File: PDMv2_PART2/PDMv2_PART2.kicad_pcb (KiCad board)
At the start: 4 copper layers, 60 x 40 mm, 4 parts

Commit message: Layout done
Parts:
- removed the REF** at (171.0, 81.0)
- removed the REF** at (121.0, 111.0)
- removed the REF** at (121.0, 81.0)
- added J1: TVP00WCI17-02P, Connector:tvp00wci17-02p, F.Cu at (81.6, 91.0)
- added J2: UMPS-08-X-X-V-S-W, UMPS-08-05.5-G-V-S-W-TR:SAMTEC_UMPS-08-X-X-V-S-W, F.Cu at (61.5, 72.3)
- added J3: UMPS-08-X-X-V-S-W, UMPS-08-05.5-G-V-S-W-TR:SAMTEC_UMPS-08-X-X-V-S-W, F.Cu at (61.5, 109.5)
- added REF**: MountingHole_3mm_Pad_Via, MountingHole:MountingHole_3mm_Pad_Via, F.Cu at (97.8, 63.7)
- added REF**: MountingHole_3mm_Pad_Via, MountingHole:MountingHole_3mm_Pad_Via, F.Cu at (98.0, 118.5)
- moved REF** 111.1 mm to (61.8, 91.0)
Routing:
- net /TSAL/HV: vias 0 -> 29
- net /SDC/ASMS: vias 0 -> 12
- net /REARBOX/DIAGPORT/BRAKE_L: vias 0 -> 26
- net /PUMP2: vias 0 -> 26
- net /PUMP1: vias 0 -> 23
- net /PC4: vias 0 -> 14
- net /PC3: vias 0 -> 13
- net /PC2: vias 0 -> 13
- net /PC1: vias 0 -> 12
- net /INVERTER 2: vias 0 -> 18
- net /INVERTER 1: vias 0 -> 21
- net /FBOX: vias 0 -> 15
- net /FAN2: vias 0 -> 34
- net /FAN1: vias 0 -> 17
- net /DASH: vias 0 -> 13
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- added copper zone on B.Cu, net /BRAKE/IR/AIR
- added copper zone on F.Cu, net /BRAKE/IR/AIR
- added copper zone on In1.Cu, net /BRAKE/IR/AIR
- added copper zone on In2.Cu, net /BRAKE/IR/AIR
- added copper zone on B.Cu, net /DASH
- added copper zone on F.Cu, net /DASH
- added copper zone on In1.Cu, net /DASH
- added copper zone on In2.Cu, net /DASH
- added copper zone on B.Cu, net /FAN1
- added copper zone on F.Cu, net /FAN1
- added copper zone on In1.Cu, net /FAN1
- added copper zone on In2.Cu, net /FAN1
- added copper zone on B.Cu, net /FAN2
- added copper zone on F.Cu, net /FAN2
- added copper zone on In1.Cu, net /FAN2
- added copper zone on In2.Cu, net /FAN2
- added copper zone on B.Cu, net /FBOX
- added copper zone on F.Cu, net /FBOX
- added copper zone on In1.Cu, net /FBOX
- added copper zone on In2.Cu, net /FBOX
- added copper zone on B.Cu, net /INVERTER 1
- added copper zone on F.Cu, net /INVERTER 1
- added copper zone on In1.Cu, net /INVERTER 1
- added copper zone on In2.Cu, net /INVERTER 1
- added copper zone on B.Cu, net /INVERTER 2
- added copper zone on F.Cu, net /INVERTER 2
- added copper zone on In1.Cu, net /INVERTER 2
- added copper zone on In2.Cu, net /INVERTER 2
- added copper zone on B.Cu, net /PC1
- added copper zone on F.Cu, net /PC1
- added copper zone on In1.Cu, net /PC1
- added copper zone on In2.Cu, net /PC1
- added copper zone on B.Cu, net /PC2
- added copper zone on F.Cu, net /PC2
- added copper zone on In1.Cu, net /PC2
- added copper zone on In2.Cu, net /PC2
- added copper zone on B.Cu, net /PC3
- added copper zone on F.Cu, net /PC3
- added copper zone on In1.Cu, net /PC3
- added copper zone on In2.Cu, net /PC3
- added copper zone on B.Cu, net /PC4
- added copper zone on F.Cu, net /PC4
- added copper zone on In1.Cu, net /PC4
- added copper zone on In2.Cu, net /PC4
- added copper zone on B.Cu, net /PUMP1
- added copper zone on F.Cu, net /PUMP1
- added copper zone on In1.Cu, net /PUMP1
- added copper zone on In2.Cu, net /PUMP1
- added copper zone on B.Cu, net /PUMP2
- added copper zone on F.Cu, net /PUMP2
- added copper zone on In1.Cu, net /PUMP2
- added copper zone on In2.Cu, net /PUMP2
- added copper zone on B.Cu, net /REARBOX/DIAGPORT/BRAKE_L
- added copper zone on F.Cu, net /REARBOX/DIAGPORT/BRAKE_L
- added copper zone on In1.Cu, net /REARBOX/DIAGPORT/BRAKE_L
- added copper zone on In2.Cu, net /REARBOX/DIAGPORT/BRAKE_L
- added copper zone on B.Cu, net /SDC/ASMS
- added copper zone on F.Cu, net /SDC/ASMS
- added copper zone on In1.Cu, net /SDC/ASMS
- added copper zone on In2.Cu, net /SDC/ASMS
- added copper zone on B.Cu, net /TSAL/HV
- added copper zone on F.Cu, net /TSAL/HV
- added copper zone on In1.Cu, net /TSAL/HV
- added copper zone on In2.Cu, net /TSAL/HV
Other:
- board size 60 x 40 mm -> 43.5 x 62 mm
- board text removed: "Template"
- board text removed: "v${REVISION}"

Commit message: Fixes
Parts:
- moved J2 0.10 mm to (61.5, 72.5)
- moved J3 0.10 mm to (61.5, 109.4)
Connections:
- J1 pad 9: /DASH -> /SDC/ASMS

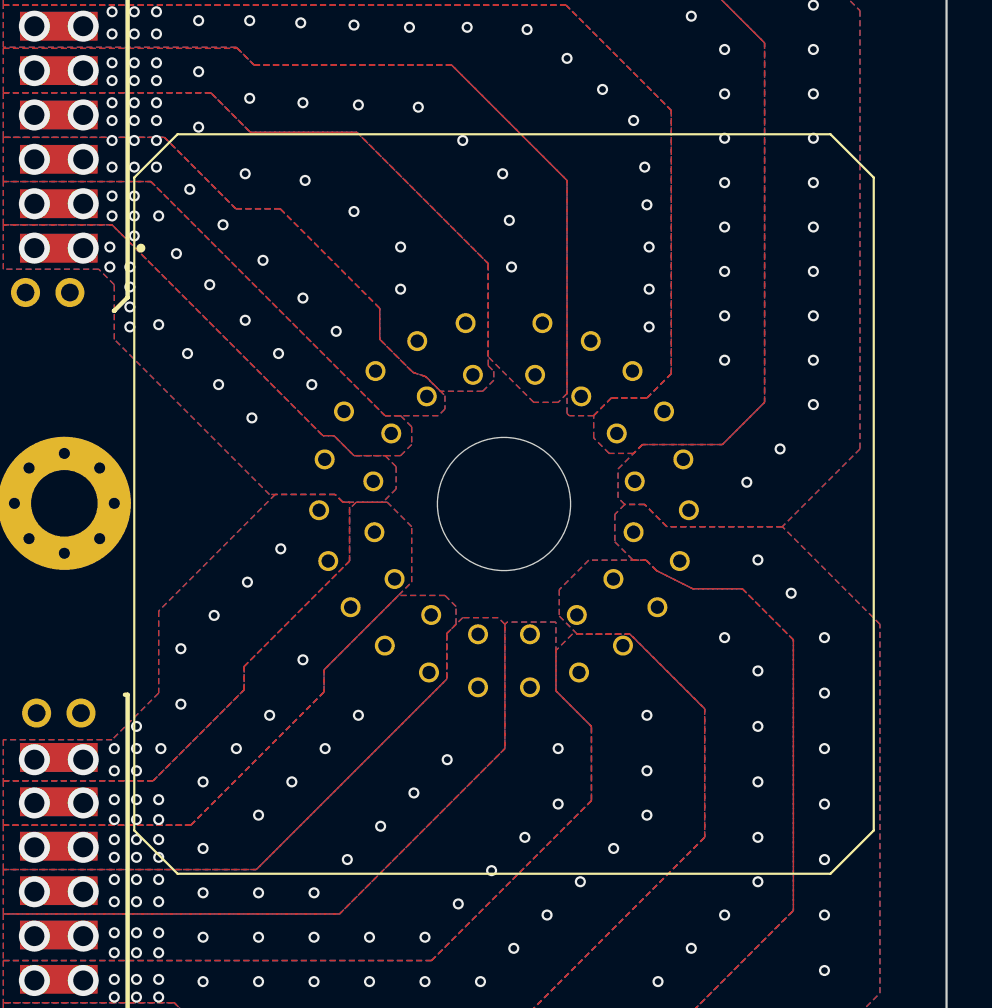
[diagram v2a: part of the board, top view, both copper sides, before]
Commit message: Fixes
Rotated connector footprint
Changed labels
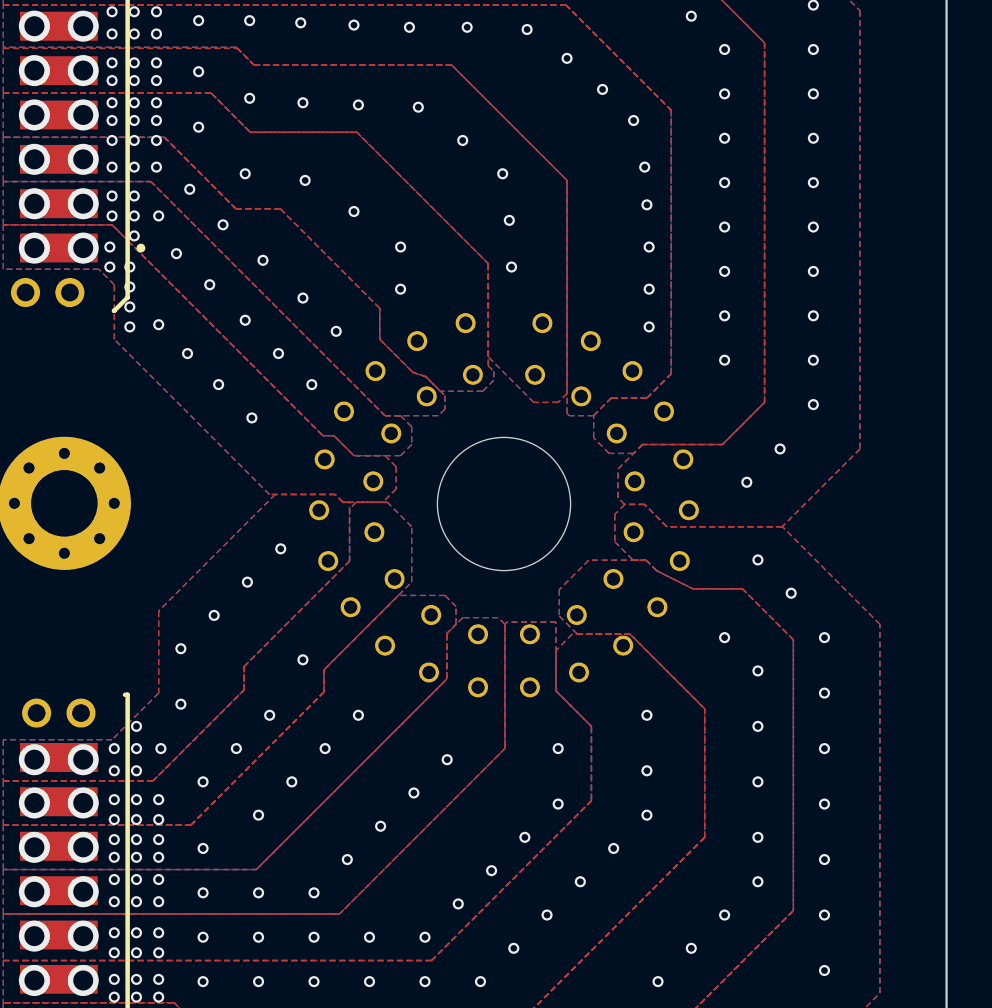
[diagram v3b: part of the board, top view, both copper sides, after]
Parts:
- J1: moved to B.Cu
- turned J1 to 180 degrees
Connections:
- J1 pad 10: /DASH -> /TSAL/HV
- J1 pad 11: /DASH -> /FAN2
- J1 pad 12: /PC1 -> /FAN2
- J1 pad 13: /PC1 -> /FAN2
- J1 pad 14: /PC2 -> /PUMP2
- J1 pad 15: /PC2 -> /PUMP2
- J1 pad 16: /PC3 -> /PUMP1
- J1 pad 17: /PC3 -> /PUMP1
- J1 pad 18: /PC4 -> /PUMP1
- J1 pad 19: /PC4 -> /FAN1
- J1 pad 2: /FBOX -> /INVERTER 2
- J1 pad 20: /PC4 -> /FAN1
- J1 pad 21: /FAN1 -> /PC4
- J1 pad 22: /FAN1 -> /PC4
- J1 pad 23: /PUMP1 -> /PC4
- J1 pad 24: /PUMP1 -> /PC3
- J1 pad 25: /PUMP1 -> /PC3
- J1 pad 26: /PUMP2 -> /PC2
- J1 pad 27: /PUMP2 -> /PC2
- J1 pad 28: /FAN2 -> /PC1
- J1 pad 29: /FAN2 -> /PC1
- J1 pad 3: /FBOX -> /INVERTER 2
- J1 pad 30: /FAN2 -> /DASH
- J1 pad 31: /TSAL/HV -> /SDC/ASMS
- J1 pad 32: /TSAL/HV -> /DASH
- J1 pad 33: /REARBOX/DIAGPORT/BRAKE_L -> /SDC/ASMS
- J1 pad 34: /REARBOX/DIAGPORT/BRAKE_L -> /SDC/ASMS
- J1 pad 35: /REARBOX/DIAGPORT/BRAKE_L -> /BRAKE/IR/AIR
- J1 pad 36: /INVERTER 1 -> /BRAKE/IR/AIR
- J1 pad 37: /INVERTER 2 -> /FBOX
- J1 pad 38: /INVERTER 1 -> /BRAKE/IR/AIR
- J1 pad 39: /INVERTER 2 -> /FBOX
- J1 pad 4: /BRAKE/IR/AIR -> /INVERTER 1
- J1 pad 5: /BRAKE/IR/AIR -> /REARBOX/DIAGPORT/BRAKE_L
- J1 pad 6: /BRAKE/IR/AIR -> /INVERTER 1
- J1 pad 7: /SDC/ASMS -> /REARBOX/DIAGPORT/BRAKE_L
- J1 pad 8: /SDC/ASMS -> /REARBOX/DIAGPORT/BRAKE_L
- J1 pad 9: /SDC/ASMS -> /TSAL/HV

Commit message: Production
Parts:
- added G***: LOGO, logos:PUTM_LOGO_15mm, F.Cu at (97.8, 92.5)
- added G***: LOGO, Logos:SignatureBox25mm, F.Cu at (79.4, 116.3)
- moved REF** 1.60 mm to (96.4, 118.3)
- moved REF** 1.34 mm to (96.4, 63.7)
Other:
- board size 43.5 x 62 mm -> 42.5 x 62 mm
- board text added: "Kacper Biadała"
- board text added: "PDM"
- board text added: "v2.0"

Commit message: Connector pads renumbered
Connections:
- J1 pad 10: /TSAL/HV -> /BRAKE/IR/AIR
- J1 pad 11: /FAN2 -> /FBOX
- J1 pad 12: /FAN2 -> /INVERTER 2
- J1 pad 13: /FAN2 -> /INVERTER 1
- J1 pad 14: /PUMP2 -> /INVERTER 1
- J1 pad 15: /PUMP2 -> /REARBOX/DIAGPORT/BRAKE_L
- J1 pad 16: /PUMP1 -> /TSAL/HV
- J1 pad 17: /PUMP1 -> /FAN2
- J1 pad 18: /PUMP1 -> /FAN2
- J1 pad 19: /FAN1 -> /PUMP2
- J1 pad 2: /INVERTER 2 -> /PC4
- J1 pad 20: /FAN1 -> /PUMP1
- J1 pad 21: /PC4 -> /PUMP1
- J1 pad 22: /PC4 -> /FAN1
- J1 pad 25: /PC3 -> /PC2
- J1 pad 26: /PC2 -> /PC1
- J1 pad 27: /PC2 -> /SDC/ASMS
- J1 pad 28: /PC1 -> /SDC/ASMS
- J1 pad 29: /PC1 -> /BRAKE/IR/AIR
- J1 pad 3: /INVERTER 2 -> /PC3
- J1 pad 30: /DASH -> /FBOX
- J1 pad 31: /SDC/ASMS -> /INVERTER 2
- J1 pad 32: /DASH -> /REARBOX/DIAGPORT/BRAKE_L
- J1 pad 33: /SDC/ASMS -> /REARBOX/DIAGPORT/BRAKE_L
- J1 pad 34: /SDC/ASMS -> /TSAL/HV
- J1 pad 35: /BRAKE/IR/AIR -> /FAN2
- J1 pad 36: /BRAKE/IR/AIR -> /PUMP2
- J1 pad 37: /FBOX -> /PUMP1
- J1 pad 38: /BRAKE/IR/AIR -> /FAN1
- J1 pad 4: /INVERTER 1 -> /PC2
- J1 pad 5: /REARBOX/DIAGPORT/BRAKE_L -> /PC1
- J1 pad 6: /INVERTER 1 -> /DASH
- J1 pad 7: /REARBOX/DIAGPORT/BRAKE_L -> /DASH
- J1 pad 8: /REARBOX/DIAGPORT/BRAKE_L -> /SDC/ASMS
- J1 pad 9: /TSAL/HV -> /BRAKE/IR/AIR

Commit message: Revert "Connector pads renumbered"
This reverts commit 75f91e02971c2a352d6d4976deddac33cb5836cf.
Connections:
- J1 pad 10: /BRAKE/IR/AIR -> /TSAL/HV
- J1 pad 11: /FBOX -> /FAN2
- J1 pad 12: /INVERTER 2 -> /FAN2
- J1 pad 13: /INVERTER 1 -> /FAN2
- J1 pad 14: /INVERTER 1 -> /PUMP2
- J1 pad 15: /REARBOX/DIAGPORT/BRAKE_L -> /PUMP2
- J1 pad 16: /TSAL/HV -> /PUMP1
- J1 pad 17: /FAN2 -> /PUMP1
- J1 pad 18: /FAN2 -> /PUMP1
- J1 pad 19: /PUMP2 -> /FAN1
- J1 pad 2: /PC4 -> /INVERTER 2
- J1 pad 20: /PUMP1 -> /FAN1
- J1 pad 21: /PUMP1 -> /PC4
- J1 pad 22: /FAN1 -> /PC4
- J1 pad 25: /PC2 -> /PC3
- J1 pad 26: /PC1 -> /PC2
- J1 pad 27: /SDC/ASMS -> /PC2
- J1 pad 28: /SDC/ASMS -> /PC1
- J1 pad 29: /BRAKE/IR/AIR -> /PC1
- J1 pad 3: /PC3 -> /INVERTER 2
- J1 pad 30: /FBOX -> /DASH
- J1 pad 31: /INVERTER 2 -> /SDC/ASMS
- J1 pad 32: /REARBOX/DIAGPORT/BRAKE_L -> /DASH
- J1 pad 33: /REARBOX/DIAGPORT/BRAKE_L -> /SDC/ASMS
- J1 pad 34: /TSAL/HV -> /SDC/ASMS
- J1 pad 35: /FAN2 -> /BRAKE/IR/AIR
- J1 pad 36: /PUMP2 -> /BRAKE/IR/AIR
- J1 pad 37: /PUMP1 -> /FBOX
- J1 pad 38: /FAN1 -> /BRAKE/IR/AIR
- J1 pad 4: /PC2 -> /INVERTER 1
- J1 pad 5: /PC1 -> /REARBOX/DIAGPORT/BRAKE_L
- J1 pad 6: /DASH -> /INVERTER 1
- J1 pad 7: /DASH -> /REARBOX/DIAGPORT/BRAKE_L
- J1 pad 8: /SDC/ASMS -> /REARBOX/DIAGPORT/BRAKE_L
- J1 pad 9: /BRAKE/IR/AIR -> /TSAL/HV
